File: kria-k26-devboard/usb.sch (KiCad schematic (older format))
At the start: 98 parts, among them U14 USB3310C-CP, U15 TPD4E05U06QDQARQ1, U16 TPD4E05U06QDQARQ1, U17 GSB3112311HR, U18 TPD4E05U06QDQARQ1, U19 TPD4E05U06QDQARQ1, U20 GSB3112311HR, U44 USB7016_KDX, U49 WE-TVS-82400152, U50 WE-TVS-82400152, U51 WE-TVS-82400152, U52 WE-TVS-82400152, U57 TPS2066TDGNRQ1, U58 TPS2066TDGNRQ1, Y4 ECS-2016MV-250-CN-TR3, Y6 ECS-2016MV-240-BN-TR3

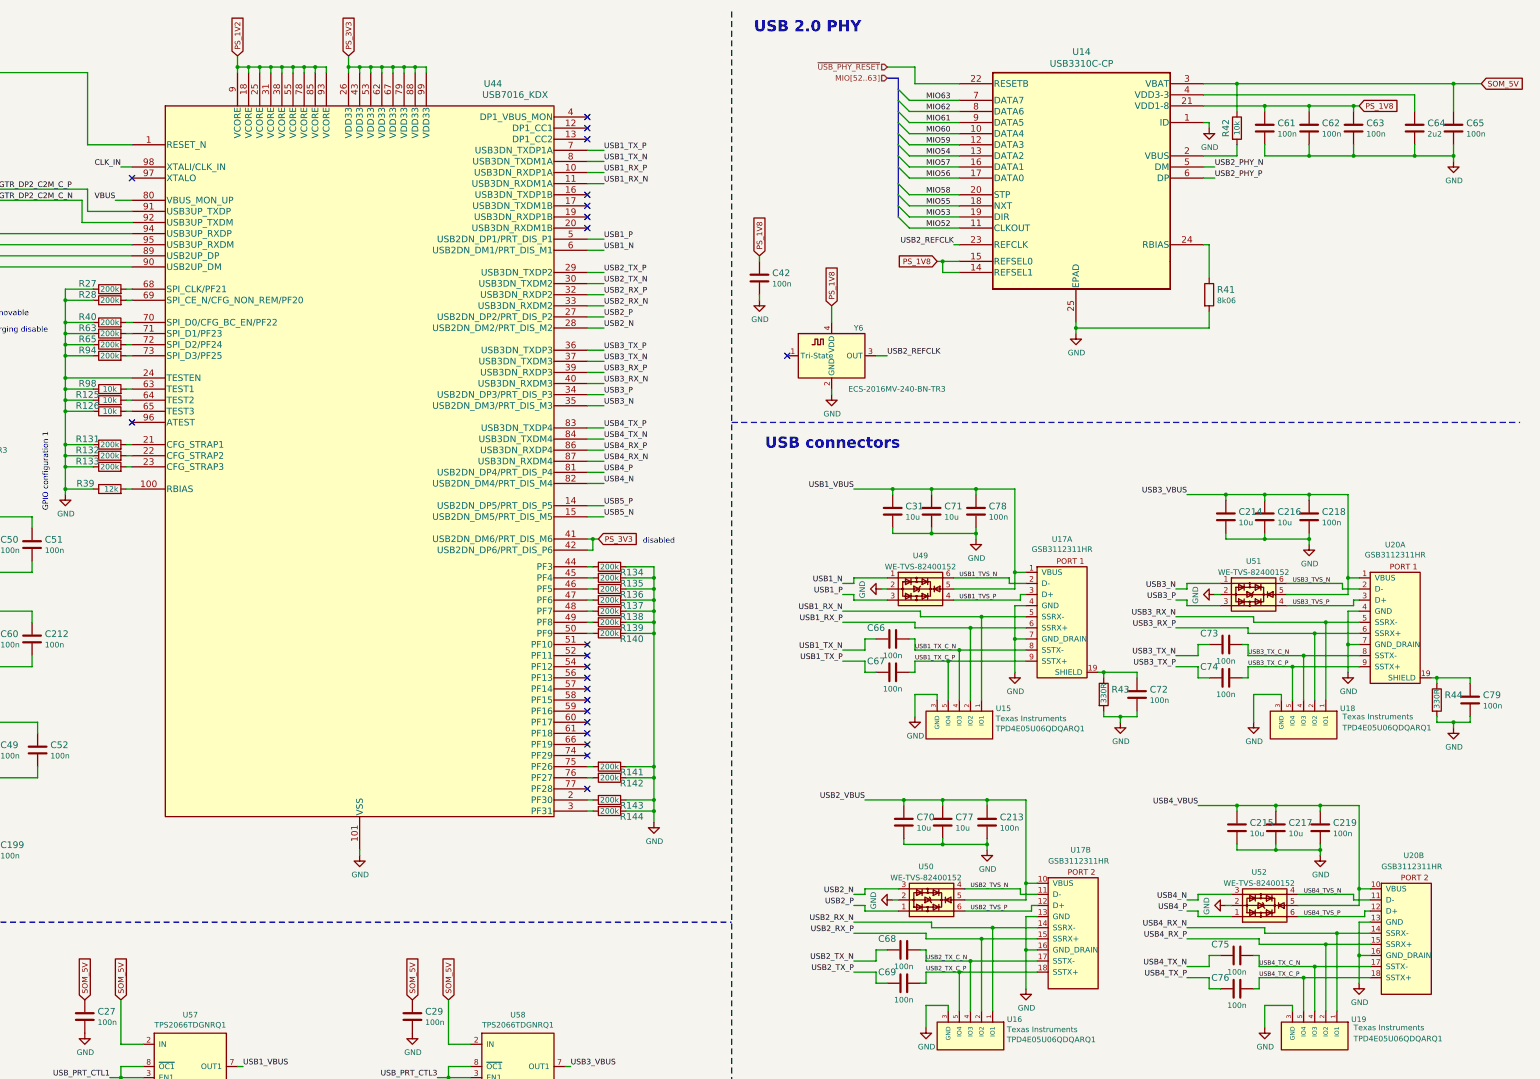
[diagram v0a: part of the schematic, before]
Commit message: Misc. signals routing, routed REF_CLK's, PS Power plane creation
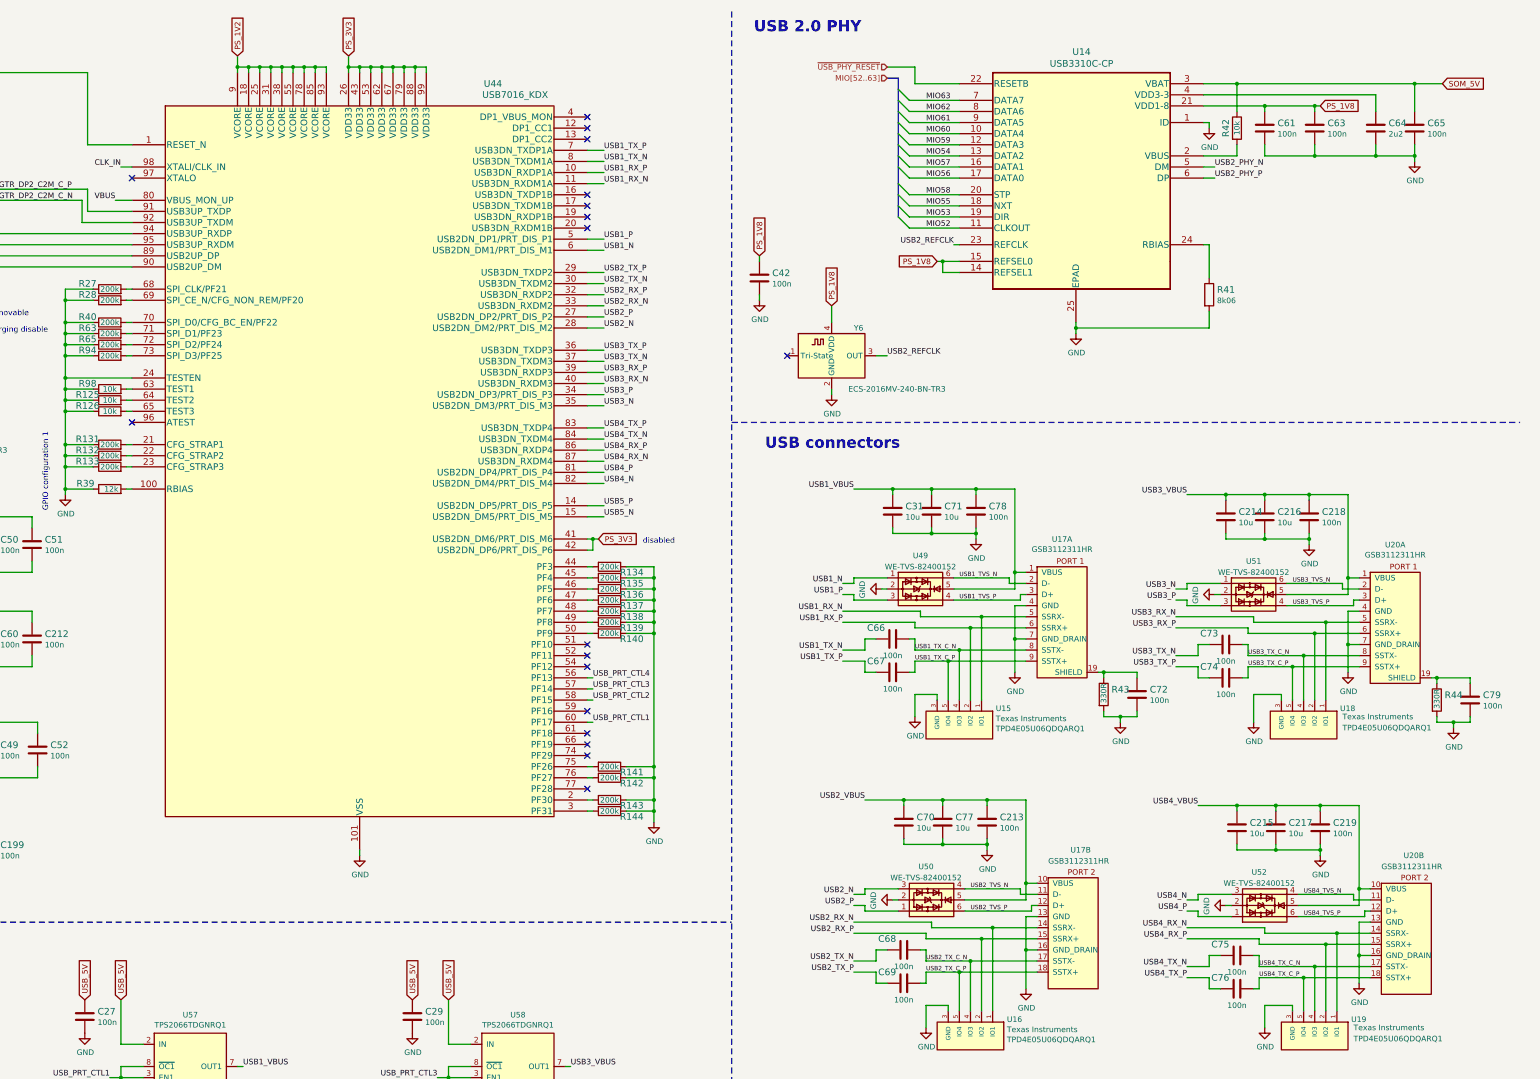
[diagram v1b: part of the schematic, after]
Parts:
- removed C62: C_100n_0402, antmicro-footprints:0402-cap, symbol antmicroCapacitors0402:C_100n_0402
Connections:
- net SOM_5V: no longer C27.1, C29.1, U57.2 (IN), U58.2 (IN)
- net USB_PRT_CTL1: now also U44.60 (PF17)
- net USB_PRT_CTL2: now also U44.58 (PF15)
- net USB_PRT_CTL3: now also U44.57 (PF14)
- net USB_PRT_CTL4: now also U44.56 (PF13)
- new net USB_5V: C27.1, C29.1, U57.2 (IN), U58.2 (IN)
- no-connect marks 23 -> 19
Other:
- moved on the sheet: C63, C64, C65
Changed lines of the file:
@@
 Wire Wire Line
 	10800 2850 10950 2850
-Text GLabel 15650 1150 2    50   Input ~ 0
+Text GLabel 15300 1150 2    50   Input ~ 0
 SOM_5V
 Wire Wire Line
-	15650 1150 15400 1150
+	15300 1150 15050 1150
 $Comp
 L antmicroCapacitors0402:C_100n_0402 C65
 U 1 1 637CC160
-P 15400 1550
-F 0 "C65" H 15515 1595 60  0000 L CNN
-F 1 "C_100n_0402" H 15400 1400 60  0001 C CNN
-F 2 "antmicro-footprints:0402-cap" H 15600 1750 60  0001 L CNN
-F 3 "" H 15400 1550 50  0001 C CNN
-F 4 "Murata" H 15600 1950 60  0001 L CNN "Manufacturer"
-F 5 "GRM155R61H104KE14D" H 15600 1850 60  0001 L CNN "MPN"
-F 6 "100n" H 15515 1497 50  0000 L CNN "Val"
-	1    15400 1550
+P 15050 1550
+F 0 "C65" H 15165 1595 60  0000 L CNN
+F 1 "C_100n_0402" H 15050 1400 60  0001 C CNN
+F 2 "antmicro-footprints:0402-cap" H 15250 1750 60  0001 L CNN
+F 3 "" H 15050 1550 50  0001 C CNN
+F 4 "Murata" H 15250 1950 60  0001 L CNN "Manufacturer"
+F 5 "GRM155R61H104KE14D" H 15250 1850 60  0001 L CNN "MPN"
+F 6 "100n" H 15165 1497 50  0000 L CNN "Val"
+	1    15050 1550
 	1    0    0    -1
 $EndComp
@@
 L antmicroCapacitors0402:C_2u2_0402 C64
 U 1 1 637D0A8C
-P 15050 1550
-F 0 "C64" H 15165 1595 60  0000 L CNN
-F 1 "C_2u2_0402" H 15050 1400 60  0001 C CNN
-F 2 "antmicro-footprints:0402-cap" H 15250 1750 60  0001 L CNN
-F 3 "" H 15050 1550 50  0001 C CNN
-F 4 "TDK" H 15250 1950 60  0001 L CNN "Manufacturer"
-F 5 "C1005X5R1A225K050BC" H 15250 1850 60  0001 L CNN "MPN"
-F 6 "2u2" H 15165 1497 50  0000 L CNN "Val"
-	1    15050 1550
+P 14700 1550
+F 0 "C64" H 14815 1595 60  0000 L CNN
+F 1 "C_2u2_0402" H 14700 1400 60  0001 C CNN
+F 2 "antmicro-footprints:0402-cap" H 14900 1750 60  0001 L CNN
+F 3 "" H 14700 1550 50  0001 C CNN
+F 4 "TDK" H 14900 1950 60  0001 L CNN "Manufacturer"
+F 5 "C1005X5R1A225K050BC" H 14900 1850 60  0001 L CNN "MPN"
+F 6 "2u2" H 14815 1497 50  0000 L CNN "Val"
+	1    14700 1550
 	1    0    0    -1
 $EndComp
 Wire Wire Line
-	13150 1250 15050 1250
+	13150 1250 14700 1250
 Wire Wire Line
-	15050 1250 15050 1400
+	14700 1250 14700 1400
 Wire Wire Line
-	15400 1400 15400 1150
-Connection ~ 15400 1150
+	15050 1400 15050 1150
+Connection ~ 15050 1150
 Wire Wire Line
-	15050 1700 15050 1800
+	14700 1700 14700 1800
 Wire Wire Line
-	15400 1800 15400 1700
+	15050 1800 15050 1700
 $Comp
 L power:GND #PWR075
 U 1 1 637D653A
-P 15400 1850
-F 0 "#PWR075" H 15400 1600 50  0001 C CNN
-F 1 "GND" H 15405 1677 50  0000 C CNN
-F 2 "" H 15400 1850 50  0001 C CNN
-F 3 "" H 15400 1850 50  0001 C CNN
-	1    15400 1850
+P 15050 1850
+F 0 "#PWR075" H 15050 1600 50  0001 C CNN
+F 1 "GND" H 15055 1677 50  0000 C CNN
+F 2 "" H 15050 1850 50  0001 C CNN
+F 3 "" H 15050 1850 50  0001 C CNN
+	1    15050 1850
 	1    0    0    -1
 $EndComp
 Wire Wire Line
-	15400 1850 15400 1800
-Wire Wire Line
-	14550 1350 14500 1350
-$Comp
-L antmicroCapacitors0402:C_100n_0402 C63
-U 1 1 637D90D2
-P 14500 1550
-F 0 "C63" H 14615 1595 60  0000 L CNN
-F 1 "C_100n_0402" H 14500 1400 60  0001 C CNN
-F 2 "antmicro-footprints:0402-cap" H 14700 1750 60  0001 L CNN
-F 3 "" H 14500 1550 50  0001 C CNN
-F 4 "Murata" H 14700 1950 60  0001 L CNN "Manufacturer"
-F 5 "GRM155R61H104KE14D" H 14700 1850 60  0001 L CNN "MPN"
-F 6 "100n" H 14615 1497 50  0000 L CNN "Val"
-	1    14500 1550
-	1    0    0    -1
-$EndComp
-$Comp
-L antmicroCapacitors0402:C_100n_0402 C62
-U 1 1 637D943F
-P 14100 1550
-F 0 "C62" H 14215 1595 60  0000 L CNN
-F 1 "C_100n_0402" H 14100 1400 60  0001 C CNN
-F 2 "antmicro-footprints:0402-cap" H 14300 1750 60  0001 L CNN
-F 3 "" H 14100 1550 50  0001 C CNN
-F 4 "Murata" H 14300 1950 60  0001 L CNN "Manufacturer"
-F 5 "GRM155R61H104KE14D" H 14300 1850 60  0001 L CNN "MPN"
-F 6 "100n" H 14215 1497 50  0000 L CNN "Val"
-	1    14100 1550
-	1    0    0    -1
-$EndComp
+	15050 1850 15050 1800
 $Comp
 L antmicroCapacitors0402:C_100n_0402 C61
@@
 Connection ~ 13700 1350
 Wire Wire Line
-	14100 1400 14100 1350
-Connection ~ 14100 1350
-Wire Wire Line
-	14100 1350 13700 1350
-Wire Wire Line
-	14500 1400 14500 1350
-Connection ~ 14500 1350
-Wire Wire Line
-	14500 1350 14100 1350
-Wire Wire Line
 	13700 1700 13700 1800
-Wire Wire Line
-	13700 1800 14100 1800
-Wire Wire Line
-	14100 1800 14100 1700
-Wire Wire Line
-	14100 1800 14500 1800
-Wire Wire Line
-	14500 1800 14500 1700
-Connection ~ 14100 1800
-Wire Wire Line
-	14500 1800 15050 1800
-Connection ~ 14500 1800
+Connection ~ 14700 1800
 Connection ~ 15050 1800
-Connection ~ 15400 1800
 Wire Wire Line
-	15050 1800 15400 1800
+	14700 1800 15050 1800
 Wire Wire Line
 	13450 1400 13450 1150
-Text GLabel 14550 1350 2    50   Input ~ 0
+Text GLabel 14200 1350 2    50   Input ~ 0
 PS_1V8
 Connection ~ 13450 1150
@@
 	13450 1150 13150 1150
 Wire Wire Line
-	13450 1150 15400 1150
+	13450 1150 15050 1150
 $Comp
 L power:GND #PWR073
@@
 Text GLabel 4450 900  1    50   Input ~ 0
 PS_1V2
-$Comp
-L antmicroInterfaceControllers:USB7016_KDX U44
-U 1 1 6268FA7C
-P 3800 1350
-F 0 "U44" H 6750 1550 60  0000 C CNN
-F 1 "USB7016_KDX" H 6950 1450 60  0000 C CNN
-F 2 "antmicro-footprints:Microchip_VQFN100_EP" H 6850 1440 60  0001 C CNN
-F 3 "https://ww1.microchip.com/downloads/en/DeviceDoc/USB7016-Data-Sheet-DS00003740B.pdf" H 3500 -1900 60  0001 C CNN
-F 4 "USB7016/KDX" H 3800 1350 50  0001 C CNN "MPN"
-F 5 "Microchip Technology" H 3800 1350 50  0001 C CNN "Manufacturer"
-	1    3800 1350
-	1    0    0    -1
-$EndComp
 Wire Wire Line
 	5250 1050 5250 1000
@@
 NoConn ~ 7600 6300
 NoConn ~ 7600 6400
-NoConn ~ 7600 6500
-NoConn ~ 7600 6600
-NoConn ~ 7600 6700
 NoConn ~ 7600 6800
-NoConn ~ 7600 6900
 NoConn ~ 7600 7000
 NoConn ~ 7600 7100
@@
 	3400 9800 3400 9400
 Text GLabel 3400 9400 1    50   Input ~ 0
-SOM_5V
+USB_5V
 $Comp
 L antmicroCapacitors0402:C_100n_0402 C27
@@
 $EndComp
 Text GLabel 3075 9400 1    50   Input ~ 0
-SOM_5V
+USB_5V
 $Comp
 L power:GND #PWR0397
@@
 	6350 9800 6350 9400
 Text GLabel 6350 9400 1    50   Input ~ 0
-SOM_5V
+USB_5V
 $Comp
 L antmicroCapacitors0402:C_100n_0402 C29
@@
 $EndComp
 Text GLabel 6025 9400 1    50   Input ~ 0
-SOM_5V
+USB_5V
 $Comp
 L power:GND #PWR0413
@@
 Connection ~ 13450 7650
 Connection ~ 14550 8400
+Text Label 7650 6900 0    50   ~ 0
+USB_PRT_CTL1
+Text Label 7650 6700 0    50   ~ 0
+USB_PRT_CTL2
+Text Label 7650 6600 0    50   ~ 0
+USB_PRT_CTL3
+Text Label 7650 6500 0    50   ~ 0
+USB_PRT_CTL4
+$Comp
+L antmicroInterfaceControllers:USB7016_KDX U44
+U 1 1 6268FA7C
+P 3800 1350
+F 0 "U44" H 6750 1550 60  0000 C CNN
+F 1 "USB7016_KDX" H 6950 1450 60  0000 C CNN
+F 2 "antmicro-footprints:Microchip_VQFN100_EP" H 6850 1440 60  0001 C CNN
+F 3 "https://ww1.microchip.com/downloads/en/DeviceDoc/USB7016-Data-Sheet-DS00003740B.pdf" H 3500 -1900 60  0001 C CNN
+F 4 "USB7016/KDX" H 3800 1350 50  0001 C CNN "MPN"
+F 5 "Microchip Technology" H 3800 1350 50  0001 C CNN "Manufacturer"
+	1    3800 1350
+	1    0    0    -1
+$EndComp
+Wire Wire Line
+	7600 6500 7650 6500
+Wire Wire Line
+	7600 6600 7650 6600
+Wire Wire Line
+	7600 6700 7650 6700
+Wire Wire Line
+	7600 6900 7650 6900
+Wire Wire Line
+	14150 1800 14700 1800
+Connection ~ 14150 1800
+Wire Wire Line
+	14150 1800 14150 1700
+Wire Wire Line
+	14200 1350 14150 1350
+Connection ~ 14150 1350
+Wire Wire Line
+	14150 1400 14150 1350
+$Comp
+L antmicroCapacitors0402:C_100n_0402 C63
+U 1 1 637D90D2
+P 14150 1550
+F 0 "C63" H 14265 1595 60  0000 L CNN
+F 1 "C_100n_0402" H 14150 1400 60  0001 C CNN
+F 2 "antmicro-footprints:0402-cap" H 14350 1750 60  0001 L CNN
+F 3 "" H 14150 1550 50  0001 C CNN
+F 4 "Murata" H 14350 1950 60  0001 L CNN "Manufacturer"
+F 5 "GRM155R61H104KE14D" H 14350 1850 60  0001 L CNN "MPN"
+F 6 "100n" H 14265 1497 50  0000 L CNN "Val"
+	1    14150 1550
+	1    0    0    -1
+$EndComp
+Wire Wire Line
+	13700 1800 14150 1800
+Wire Wire Line
+	13700 1350 14150 1350
 Wire Bus Line
 	10400 1100 10400 2350

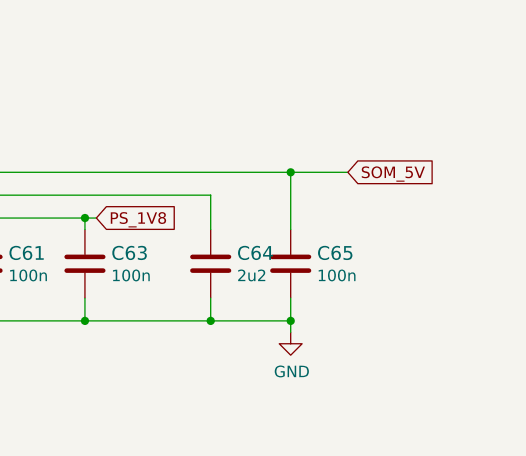
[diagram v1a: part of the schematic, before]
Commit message: Fixed possible FTDI-USB backfeeding issue, finished PS and FTDI power planes creation, finished routing of FTDI/Debug part
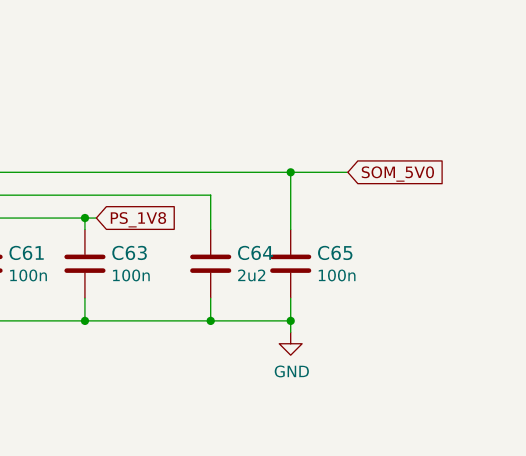
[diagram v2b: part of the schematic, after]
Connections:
- net SOM_5V renamed SOM_5V0
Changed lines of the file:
@@
 	10800 2850 10950 2850
 Text GLabel 15300 1150 2    50   Input ~ 0
-SOM_5V
+SOM_5V0
 Wire Wire Line
 	15300 1150 15050 1150

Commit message: Optimization of power planes, fixed missing capacitors on USB 3.0, unify shields, polishing of layout
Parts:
- removed C72: C_100n_0402, antmicro-footprints:0402-cap, symbol antmicroCapacitors0402:C_100n_0402
- removed R43, R44: R_330R_0402, antmicro-footprints:0402-res, symbol antmicroResistors0402:R_330R_0402
- added C185: C_100n_0402, antmicro-footprints:0402-cap, symbol antmicroCapacitors0402:C_100n_0402
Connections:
- net GND: no longer C79.2
- net GTR_DP2_M2C_N: now also C185.2; no longer U44.95 (USB3UP_RXDM)
- net GTR_DP2_M2C_P: now also C79.2; no longer U44.94 (USB3UP_RXDP)
- net SH_UP: now reaches U17.19 (SHIELD)
- net SH_UP: now also U20.19 (SHIELD)
- net GTR_DP2_M2C_C_P: now reaches C79.1
- net GTR_DP2_M2C_C_P: now also U44.94 (USB3UP_RXDP); no longer U20.19 (SHIELD)
- new net GTR_DP2_M2C_C_N: C185.1, U44.95 (USB3UP_RXDM)
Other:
- moved on the sheet: C55, C56, R25, R26

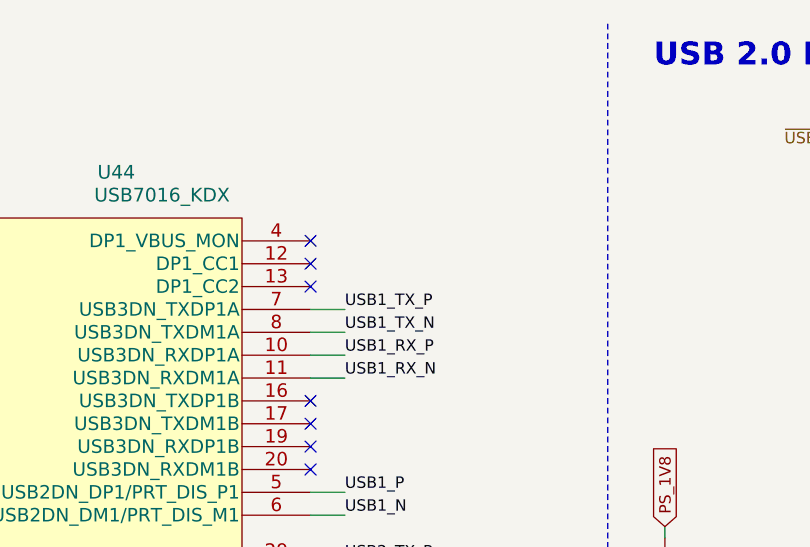
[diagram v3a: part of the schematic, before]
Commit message: Finished length matching and deskewing high speed traces
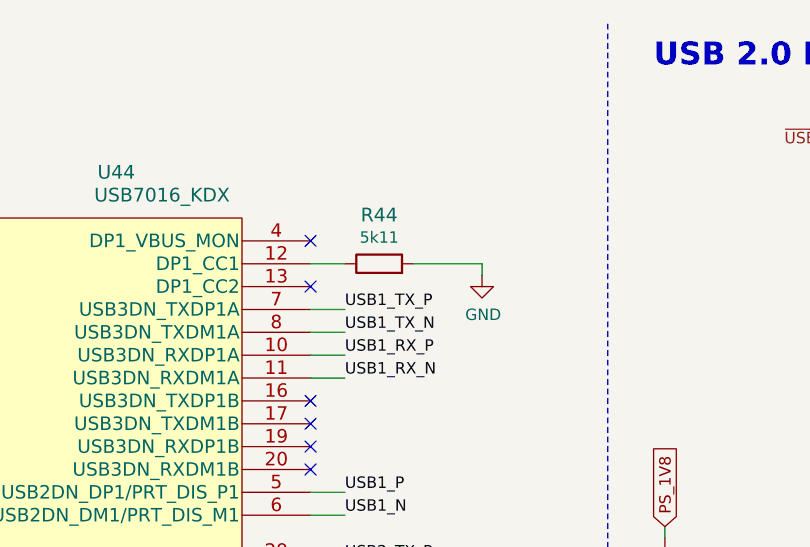
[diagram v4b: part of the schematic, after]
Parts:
- added R44: R_5k11_0402, antmicro-footprints:0402-res, symbol antmicroResistors0402:R_5k11_0402
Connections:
- net GND: now also R44.2
- net at U44.12 (DP1_CC1): now also R44.1
- no-connect marks 19 -> 18
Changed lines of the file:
@@
-	1    0    0    -1
-$EndComp
-$Comp
-L power:GND #PWR067
-U 1 1 65B92F5E
-P 9150 3100
-F 0 "#PWR067" H 9150 2850 50  0001 C CNN
-F 1 "GND" H 9155 2927 50  0000 C CNN
-F 2 "" H 9150 3100 50  0001 C CNN
-F 3 "" H 9150 3100 50  0001 C CNN
-	1    9150 3100
 	1    0    0    -1
 $EndComp
@@
 Connection ~ 2200 6400
 NoConn ~ 7600 1650
-NoConn ~ 7600 1550
 NoConn ~ 7600 1450
 NoConn ~ 7600 2150
@@
 Wire Wire Line
 	2800 2700 2800 2950
+$Comp
+L antmicroResistors0402:R_5k11_0402 R44
+U 1 1 6275E9EA
+P 7900 1550
+F 0 "R44" H 7900 1763 60  0000 C CNN
+F 1 "R_5k11_0402" H 7900 1400 60  0001 C CNN
+F 2 "antmicro-footprints:0402-res" H 8100 1750 60  0001 L CNN
+F 3 "" H 7900 1550 50  0001 C CNN
+F 4 "WALSIN" H 8100 1950 60  0001 L CNN "Manufacturer"
+F 5 "WR04X5111FTL" H 8100 1850 60  0001 L CNN "MPN"
+F 6 "5k11" H 7900 1665 50  0000 C CNN "Val"
+	1    7900 1550
+	1    0    0    -1
+$EndComp
+Wire Wire Line
+	7600 1550 7750 1550
+$Comp
+L power:GND #PWR067
+U 1 1 65B92F5E
+P 9150 3100
+F 0 "#PWR067" H 9150 2850 50  0001 C CNN
+F 1 "GND" H 9155 2927 50  0000 C CNN
+F 2 "" H 9150 3100 50  0001 C CNN
+F 3 "" H 9150 3100 50  0001 C CNN
+	1    9150 3100
+	1    0    0    -1
+$EndComp
+$Comp
+L power:GND #PWR0298
+U 1 1 62838397
+P 8350 1600
+F 0 "#PWR0298" H 8350 1350 50  0001 C CNN
+F 1 "GND" H 8355 1427 50  0000 C CNN
+F 2 "" H 8350 1600 50  0001 C CNN
+F 3 "" H 8350 1600 50  0001 C CNN
+	1    8350 1600
+	1    0    0    -1
+$EndComp
+Wire Wire Line
+	8050 1550 8350 1550
+Wire Wire Line
+	8350 1550 8350 1600
 Wire Bus Line
 	10400 1100 10400 2350

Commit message: Fixed missing USB - M2 connection, finishing touches of PCB
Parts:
- added TP8: TP_SMD_0_75MM, antmicro-footprints:Testpoint_smd_0_75mm, symbol antmicroTestPoints:TP_SMD_0_75MM
- renumbered C53 to C45, C44 to C46, C54 to C47, C43 to C48, C190 to C49, C46 to C50, C57 to C51, C45 to C52, C193 to C53, C48 to C54, C59 to C55, C47 to C56, C196 to C57, C55 to C58, C56 to C59, C79 to C60, C185 to C61, C50 to C62, C60 to C63, C49 to C64, C199 to C65, C51 to C66, C212 to C67, C52 to C68, C27 to C69, C29 to C70, C42 to C71, C31 to C72, C66 to C73, C67 to C74, C70 to C75, C68 to C76, C69 to C77, C71 to C78, C77 to C79, C78 to C80, C213 to C81, C214 to C82, C73 to C83, C74 to C84, C215 to C85, C75 to C86, C76 to C87, C61 to C88, C216 to C89, C217 to C90, C218 to C91, C63 to C92, C219 to C93, C64 to C94, C65 to C95, R25 to R40, R26 to R41, R27 to R42, R28 to R43, R40 to R44, R63 to R45, R65 to R46, R94 to R47, R98 to R48, R125 to R49, R126 to R50, R131 to R51, R132 to R52, R133 to R53, R39 to R54, R134 to R55, R135 to R56, R136 to R57, R137 to R58, R138 to R59, R139 to R60, R140 to R61, R141 to R62, R142 to R63, R143 to R64, R144 to R65, R44 to R66, R41 to R67, R42 to R68, U57 to U16, U44 to U17, U58 to U18, U49 to U19, U50 to U20, U14 to U21, U15 to U22, U16 to U23, U17 to U24, U51 to U25, U52 to U26, U18 to U27, U19 to U28, U20 to U29, Y6 to Y5
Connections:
- net VBUS: now also TP8.1
